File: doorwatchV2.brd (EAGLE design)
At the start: 91.4 x 77.5 mm, 43 parts, among them IC1 LM2576S-5.0, IC2 MAX3232CPE, K1 FINDER-43.61, Q1 IRLZ44Z, T1 BC847, T2 BC847, T3 BC847, T4 BC847, X1 MKDSN1,5/2-5,08, X2 D-SUB9-H2M09RA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

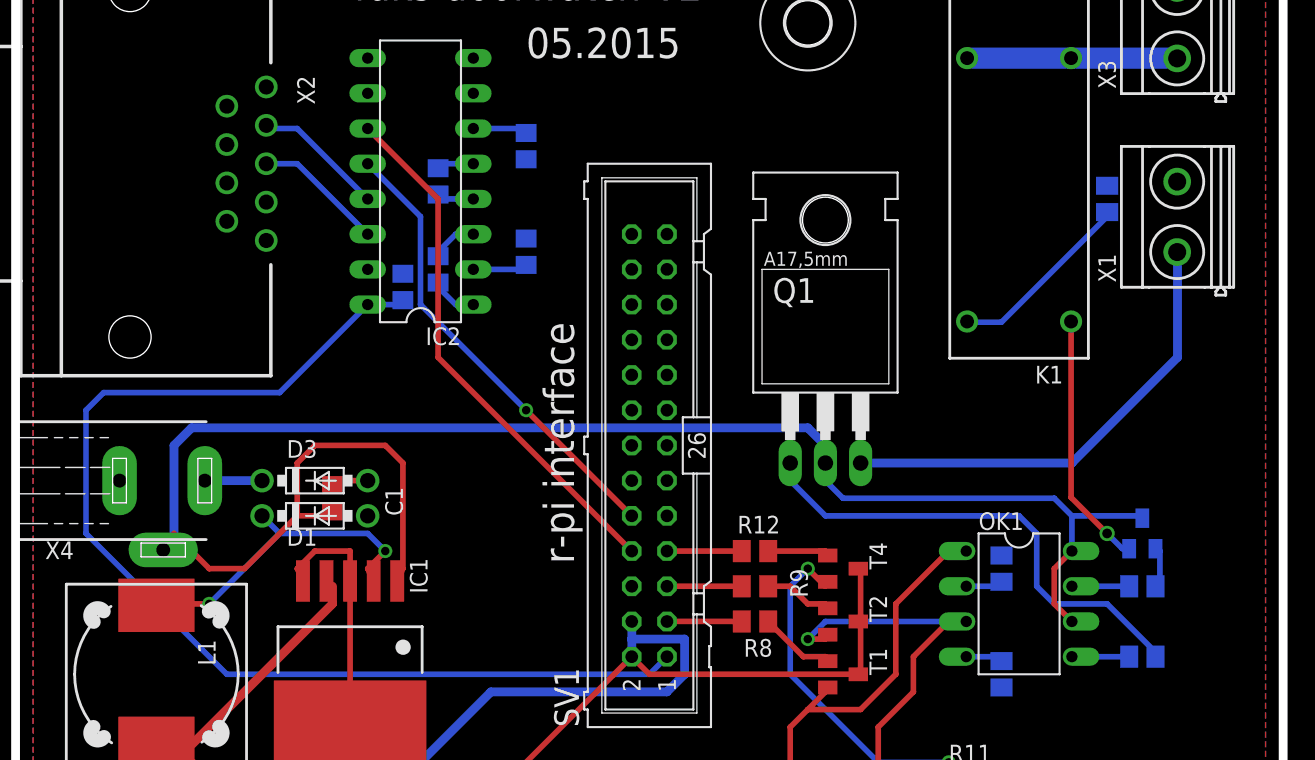
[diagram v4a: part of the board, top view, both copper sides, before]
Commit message: added some text components to board to sign connectors
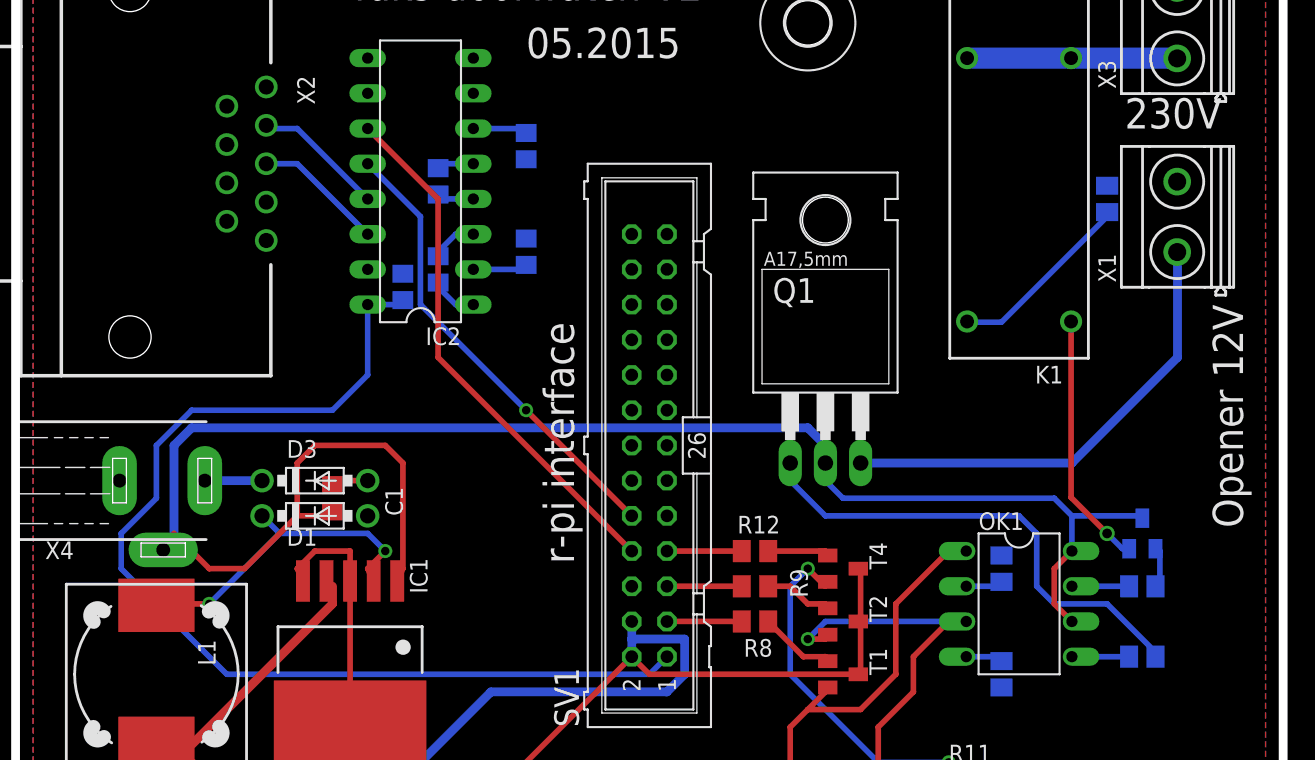
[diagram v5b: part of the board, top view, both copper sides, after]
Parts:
- R12, R3, R7: value 10k -> 1k
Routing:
- net +3V3: track 81.9 -> 78.3 mm
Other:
- board text added: "Opener 12V"
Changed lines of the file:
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@@
 <text x="36.83" y="72.39" size="2.1844" layer="25" rot="R270">r-pi interface</text>
 <text x="35.56" y="91.44" size="2.1844" layer="25">05.2015</text>
+<text x="85.09" y="73.66" size="2.1844" layer="21" rot="R270">Opener 12V</text>
+<text x="78.74" y="86.36" size="2.1844" layer="21">230V</text>
 </plain>
 <attributes>
@@
 <attribute name="VALUE" x="58.42" y="34.29" size="1.27" layer="27" rot="R270"/>
 </element>
-<element name="R3" library="rcl" package="M0805" value="10k" x="80.01" y="48.26" rot="MR180"/>
+<element name="R3" library="rcl" package="M0805" value="1k" x="80.01" y="48.26" rot="MR180"/>
 <element name="R4" library="rcl" package="M0805" value="330" x="54.61" y="38.1" smashed="yes" rot="R270">
 <attribute name="NAME" x="52.07" y="39.37" size="1.27" layer="25" rot="R270"/>
@@
 <attribute name="OC_FARNELL" value="unknown" x="133.35" y="124.46" size="1.778" layer="27" rot="R90" display="off"/>
 </element>
-<element name="R7" library="rcl" package="M0805" value="10k" x="80.01" y="53.34" rot="MR180"/>
+<element name="R7" library="rcl" package="M0805" value="1k" x="80.01" y="53.34" rot="MR180"/>
 <element name="X3" library="con-phoenix-508" package="MKDSN1,5/2-5,08" value="MKDSN1,5/2-5,08" x="82.55" y="93.98" rot="R90">
 <attribute name="OC_NEWARK" value="30M2397" x="115.57" y="128.27" size="1.778" layer="27" rot="R90" display="off"/>
@@
 </element>
 <element name="T4" library="transistor" package="SOT23" value="BC847" x="58.42" y="54.61" rot="R270"/>
-<element name="R12" library="rcl" package="M0805" value="10k" x="52.07" y="55.88"/>
+<element name="R12" library="rcl" package="M0805" value="1k" x="52.07" y="55.88"/>
 <element name="H1" library="holes" package="3,2" value="MOUNT-HOLE3.2" x="8.89" y="33.02"/>
 <element name="H2" library="holes" package="3,2" value="MOUNT-HOLE3.2" x="55.88" y="93.98"/>
@@
 <wire x1="44.45" y1="46.99" x2="45.72" y2="48.26" width="0.4064" layer="16"/>
 <wire x1="13.97" y1="46.99" x2="44.45" y2="46.99" width="0.4064" layer="16"/>
-<wire x1="3.81" y1="57.15" x2="13.97" y2="46.99" width="0.4064" layer="16"/>
-<wire x1="24.13" y1="73.66" x2="17.78" y2="67.31" width="0.4064" layer="16"/>
-<wire x1="17.78" y1="67.31" x2="5.08" y2="67.31" width="0.4064" layer="16"/>
-<wire x1="5.08" y1="67.31" x2="3.81" y2="66.04" width="0.4064" layer="16"/>
-<wire x1="3.81" y1="66.04" x2="3.81" y2="57.15" width="0.4064" layer="16"/>
+<wire x1="13.97" y1="46.99" x2="6.35" y2="54.61" width="0.4064" layer="16"/>
+<wire x1="6.35" y1="54.61" x2="6.35" y2="57.15" width="0.4064" layer="16"/>
+<wire x1="6.35" y1="57.15" x2="8.89" y2="59.69" width="0.4064" layer="16"/>
+<wire x1="8.89" y1="59.69" x2="8.89" y2="63.5" width="0.4064" layer="16"/>
+<wire x1="8.89" y1="63.5" x2="11.43" y2="66.04" width="0.4064" layer="16"/>
+<wire x1="11.43" y1="66.04" x2="21.59" y2="66.04" width="0.4064" layer="16"/>
+<wire x1="21.59" y1="66.04" x2="24.13" y2="68.58" width="0.4064" layer="16"/>
+<wire x1="24.13" y1="68.58" x2="24.13" y2="73.66" width="0.4064" layer="16"/>
 </signal>
 <signal name="GPIO2">
@@
 <contactref element="Q1" pad="S"/>
 <contactref element="X1" pad="1"/>
-<wire x1="68.58" y1="71.12" x2="59.69" y2="62.23" width="0" layer="19" extent="1-16"/>
-<wire x1="76.2" y1="71.12" x2="68.58" y2="71.12" width="0" layer="19" extent="1-16"/>
-<wire x1="59.69" y1="62.23" x2="76.2" y2="71.12" width="0" layer="19" extent="1-16"/>
 <wire x1="82.55" y1="77.47" x2="82.525" y2="77.4489" width="0.4064" layer="16"/>
 <wire x1="82.55" y1="77.47" x2="82.55" y2="69.85" width="0.635" layer="16"/>

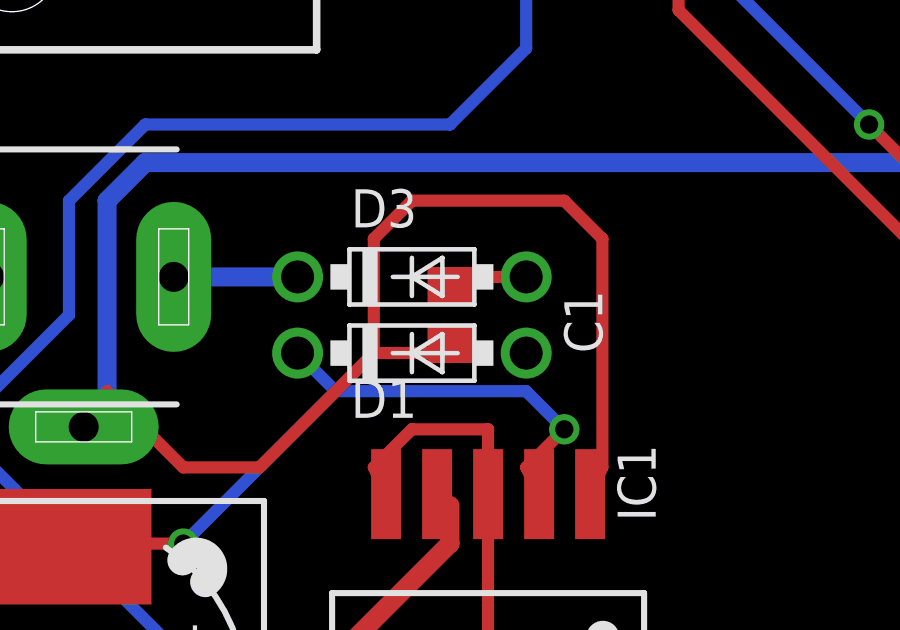
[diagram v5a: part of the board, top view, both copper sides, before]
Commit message: changed C1 condensator to an elko type
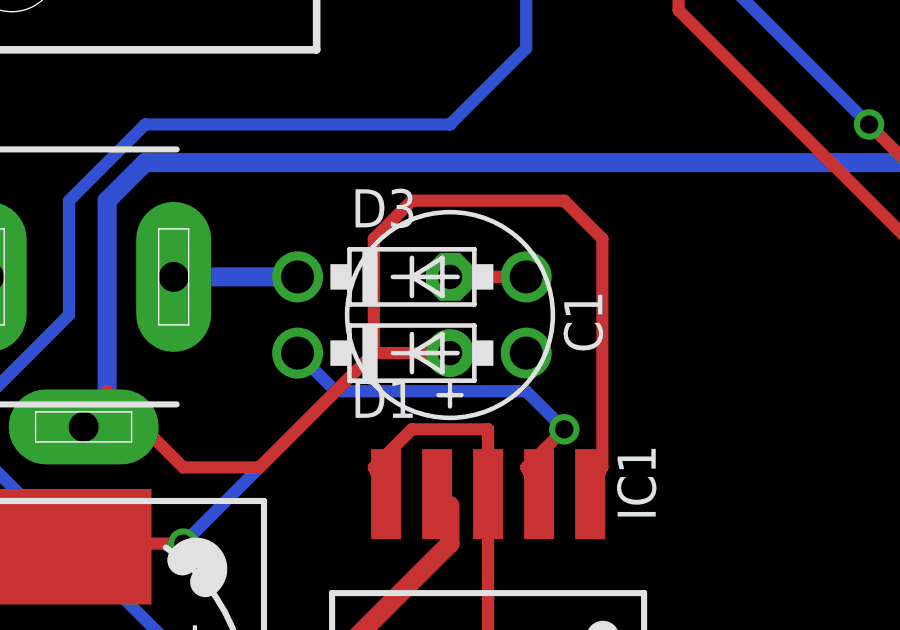
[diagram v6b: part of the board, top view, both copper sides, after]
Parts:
- C1: device rcl:C0805 -> rcl:E2,5-7
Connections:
- net +12V: now also C1.+; no longer C1.1
- net GND: now also C1.-; no longer C1.2
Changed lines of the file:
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@@
 <?xml version="1.0" encoding="utf-8"?>
 <!DOCTYPE eagle SYSTEM "eagle.dtd">
-<eagle version="6.0">
+<eagle version="7.3.0">
 <drawing>
 <settings>
@@
 <layer number="17" name="Pads" color="2" fill="1" visible="yes" active="yes"/>
 <layer number="18" name="Vias" color="2" fill="1" visible="yes" active="yes"/>
-<layer number="19" name="Unrouted" color="6" fill="1" visible="yes" active="yes"/>
+<layer number="19" name="Unrouted" color="6" fill="1" visible="no" active="yes"/>
 <layer number="20" name="Dimension" color="15" fill="1" visible="yes" active="yes"/>
 <layer number="21" name="tPlace" color="7" fill="1" visible="yes" active="yes"/>
-<layer number="22" name="bPlace" color="7" fill="1" visible="yes" active="yes"/>
+<layer number="22" name="bPlace" color="7" fill="1" visible="no" active="yes"/>
 <layer number="23" name="tOrigins" color="15" fill="1" visible="no" active="yes"/>
 <layer number="24" name="bOrigins" color="15" fill="1" visible="no" active="yes"/>
 <layer number="25" name="tNames" color="7" fill="1" visible="yes" active="yes"/>
-<layer number="26" name="bNames" color="7" fill="1" visible="yes" active="yes"/>
+<layer number="26" name="bNames" color="7" fill="1" visible="no" active="yes"/>
 <layer number="27" name="tValues" color="7" fill="1" visible="no" active="yes"/>
 <layer number="28" name="bValues" color="7" fill="1" visible="no" active="yes"/>
@@
 <wire x1="90.17" y1="24.13" x2="-1.27" y2="24.13" width="0.635" layer="20"/>
 <wire x1="-1.27" y1="24.13" x2="-1.27" y2="101.6" width="0.635" layer="20"/>
-<dimension x1="-1.27" y1="101.6" x2="90.17" y2="101.6" x3="44.45" y3="105.41" layer="48"/>
-<dimension x1="-1.27" y1="24.13" x2="-1.27" y2="101.6" x3="-10.16" y3="62.865" layer="48"/>
+<dimension x1="-1.27" y1="101.6" x2="90.17" y2="101.6" x3="44.45" y3="105.41" textsize="3.5" layer="48"/>
+<dimension x1="-1.27" y1="24.13" x2="-1.27" y2="101.6" x3="-10.16" y3="62.865" textsize="3.5" layer="48"/>
 <text x="48.26" y="97.79" size="2.1844" layer="25" rot="R180">fuks doorwatch V2</text>
 <text x="36.83" y="72.39" size="2.1844" layer="25" rot="R270">r-pi interface</text>
@@
 </class>
 </classes>
-<designrules>
+<designrules name="default">
 <description language="de">&lt;b&gt;EAGLE Design Rules&lt;/b&gt;
 &lt;p&gt;
@@
 <pass name="Default">
 <param name="RoutingGrid" value="50mil"/>
+<param name="AutoGrid" value="1"/>
+<param name="Efforts" value="0"/>
+<param name="TopRouterVariant" value="1"/>
 <param name="tpViaShape" value="round"/>
 <param name="PrefDir.1" value="|"/>
@@
 <attribute name="VALUE" x="18.288" y="55.499" size="1.27" layer="27" ratio="10"/>
 </element>
-<element name="C1" library="rcl" package="C0805" value="100uF" x="21.59" y="59.69" smashed="yes" rot="R90">
+<element name="C1" library="rcl" package="E2,5-7" value="100uF" x="21.59" y="59.69" smashed="yes" rot="R90">
 <attribute name="NAME" x="26.67" y="58.42" size="1.27" layer="25" rot="R90"/>
 <attribute name="VALUE" x="24.13" y="58.42" size="1.27" layer="27" rot="R90"/>
@@
 <contactref element="D1" pad="A"/>
 <contactref element="C2" pad="-"/>
-<contactref element="C1" pad="2"/>
+<contactref element="C1" pad="-"/>
 <contactref element="D3" pad="A"/>
 <contactref element="SV1" pad="6"/>
@@
 <wire x1="25.4" y1="31.75" x2="31.75" y2="31.75" width="0.4064" layer="1"/>
 <wire x1="24.13" y1="60.96" x2="21.59" y2="60.96" width="0.4064" layer="1"/>
-<wire x1="21.59" y1="60.96" x2="21.59" y2="60.64" width="0.4064" layer="1"/>
 <wire x1="31.75" y1="31.75" x2="54.61" y2="31.75" width="0.4064" layer="1"/>
 <wire x1="54.61" y1="31.75" x2="54.61" y2="31.97" width="0.4064" layer="1"/>
@@
 <signal name="+12V">
 <contactref element="IC1" pad="1"/>
-<contactref element="C1" pad="1"/>
+<contactref element="C1" pad="+"/>
 <contactref element="X4" pad="3"/>
 <contactref element="OK1" pad="6"/>
@@
 <wire x1="12.7" y1="54.61" x2="15.24" y2="54.61" width="0.4064" layer="1"/>
 <wire x1="10.16" y1="57.15" x2="12.7" y2="54.61" width="0.4064" layer="1"/>
-<wire x1="21.59" y1="58.42" x2="21.59" y2="58.74" width="0.4064" layer="1"/>
 <wire x1="10.16" y1="57.15" x2="9.38" y2="55.96" width="0.4064" layer="1"/>
 <wire x1="26.67" y1="62.23" x2="26.67" y2="54.61" width="0.4064" layer="1"/>
